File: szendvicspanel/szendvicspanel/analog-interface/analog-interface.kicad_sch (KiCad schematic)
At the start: 12 parts, among them J1 AudioJack3, J4 Conn_01x04_Pin, J5 Conn_01x04_Pin, U3 TL072

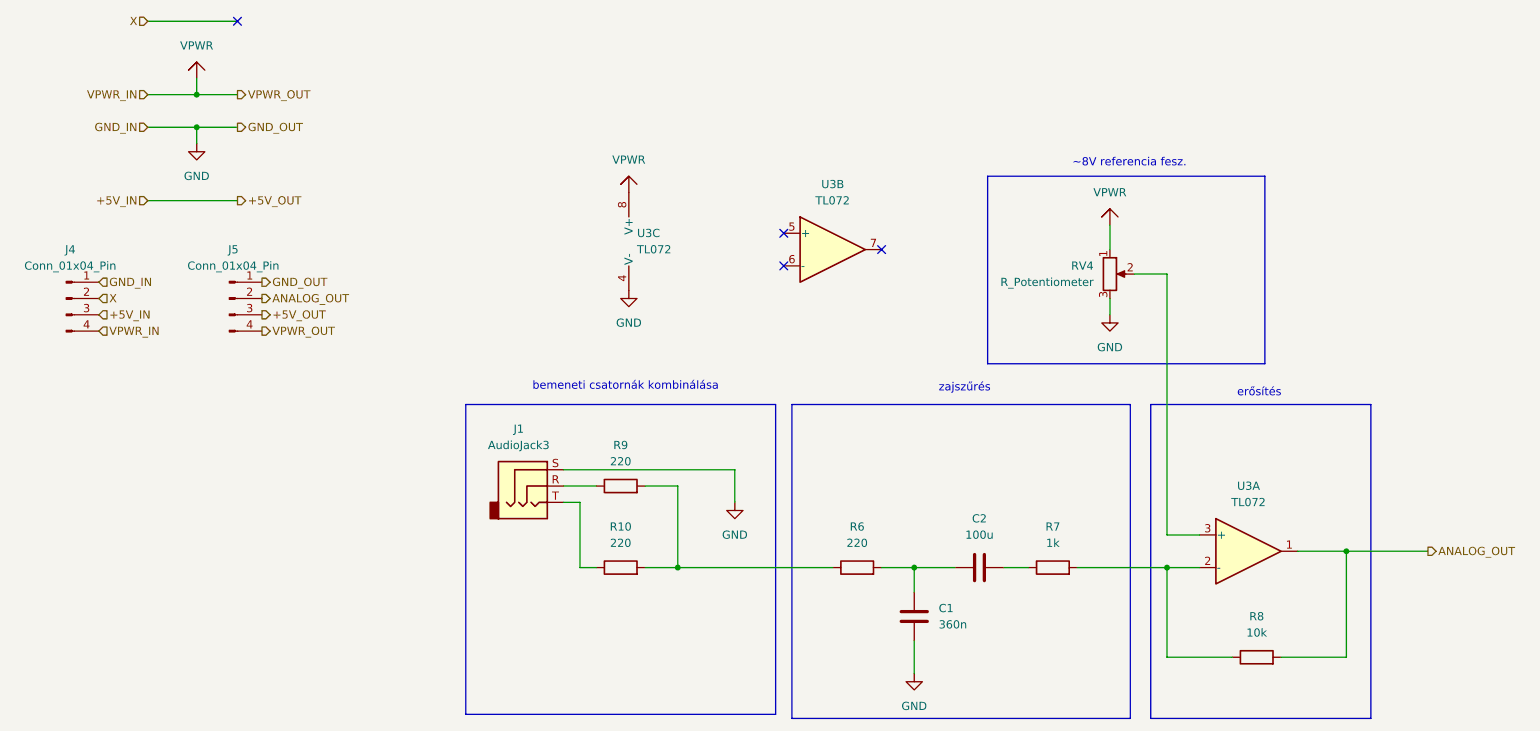
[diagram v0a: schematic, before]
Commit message: Átstrukturálás hierarchikus PCB-hez
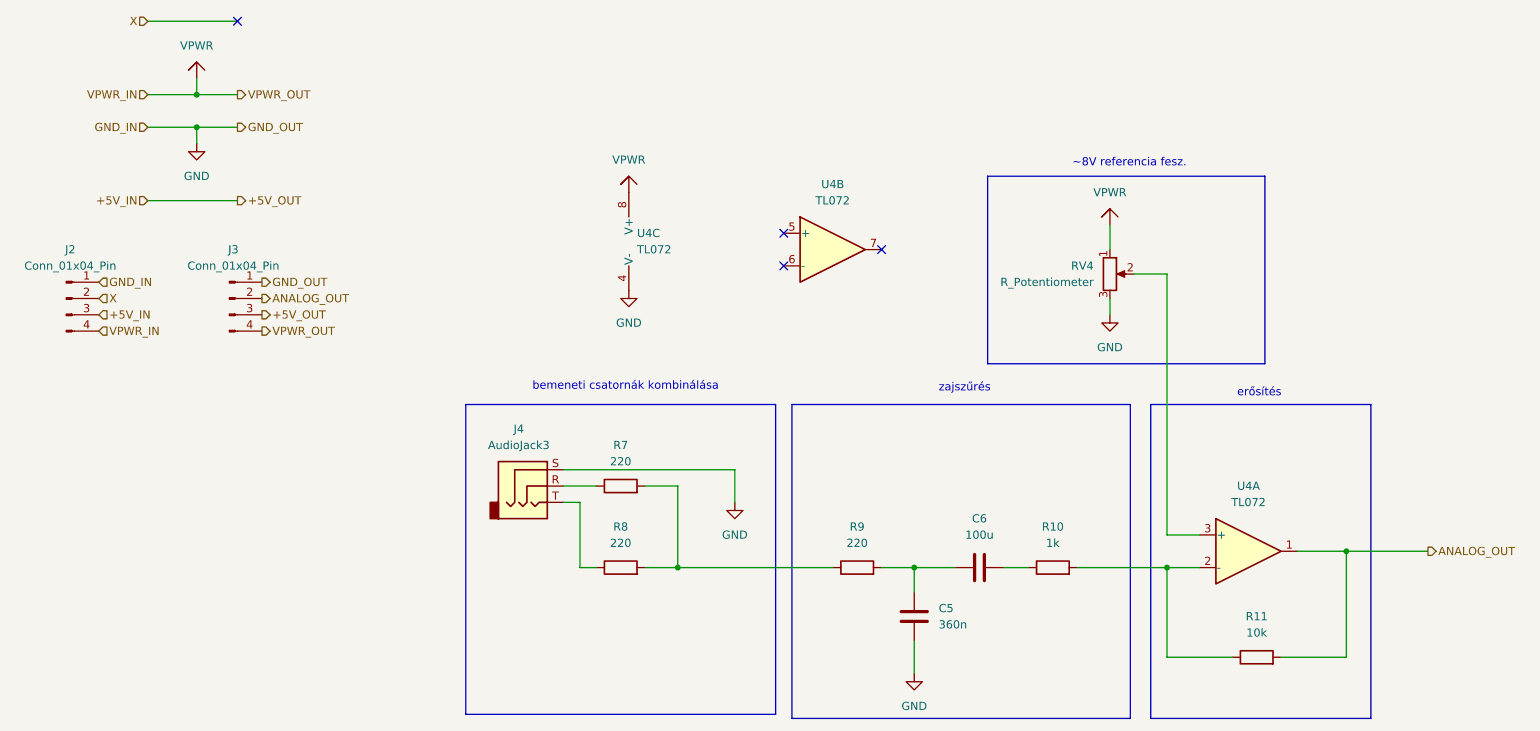
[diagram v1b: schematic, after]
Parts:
- renumbered C1 to C5, C2 to C6, J4 to J2, J5 to J3, J1 to J4, R7 to R10, R8 to R11, R9 to R7, R10 to R8, R6 to R9, U3 to U4
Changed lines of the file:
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@@
 		(dnp no)
 		(fields_autoplaced yes)
-		(property "Reference" "#PWR012"
+		(property "Reference" "#PWR022"
 			(at 186.69 77.47 0)
 			(effects
@@
 			(project "szendvicspanel"
 				(path "/2e536be4-7a69-4064-ab31-c73232c2dcfe/956847b2-170c-4df3-ad01-276d0d878286"
-					(reference "#PWR012")
+					(reference "#PWR022")
 					(unit 1)
 				)
@@
 		(dnp no)
 		(fields_autoplaced yes)
-		(property "Reference" "R9"
+		(property "Reference" "R7"
 			(at 110.49 91.44 90)
 			(effects
@@
 			(project ""
 				(path "/2e536be4-7a69-4064-ab31-c73232c2dcfe/956847b2-170c-4df3-ad01-276d0d878286"
-					(reference "R9")
+					(reference "R7")
 					(unit 1)
 				)
@@
 		(dnp no)
 		(fields_autoplaced yes)
-		(property "Reference" "R6"
+		(property "Reference" "R9"
 			(at 147.32 104.14 90)
 			(effects
@@
 			(project ""
 				(path "/2e536be4-7a69-4064-ab31-c73232c2dcfe/956847b2-170c-4df3-ad01-276d0d878286"
-					(reference "R6")
+					(reference "R9")
 					(unit 1)
 				)
@@
 		(dnp no)
 		(fields_autoplaced yes)
-		(property "Reference" "J5"
+		(property "Reference" "J3"
 			(at 50.165 60.96 0)
 			(effects
@@
 			(project "szendvicspanel"
 				(path "/2e536be4-7a69-4064-ab31-c73232c2dcfe/956847b2-170c-4df3-ad01-276d0d878286"
-					(reference "J5")
+					(reference "J3")
 					(unit 1)
 				)
@@
 		(dnp no)
 		(fields_autoplaced yes)
-		(property "Reference" "R10"
+		(property "Reference" "R8"
 			(at 110.49 104.14 90)
 			(effects
@@
 			(project "szendvicspanel"
 				(path "/2e536be4-7a69-4064-ab31-c73232c2dcfe/956847b2-170c-4df3-ad01-276d0d878286"
-					(reference "R10")
+					(reference "R8")
 					(unit 1)
 				)
@@
 		(on_board yes)
 		(dnp no)
-		(property "Reference" "#PWR020"
+		(property "Reference" "#PWR019"
 			(at 111.76 73.66 0)
 			(effects
@@
 			(project "szendvicspanel"
 				(path "/2e536be4-7a69-4064-ab31-c73232c2dcfe/956847b2-170c-4df3-ad01-276d0d878286"
-					(reference "#PWR020")
+					(reference "#PWR019")
 					(unit 1)
 				)
@@
 		(dnp no)
 		(fields_autoplaced yes)
-		(property "Reference" "C2"
+		(property "Reference" "C6"
 			(at 166.37 102.87 90)
 			(effects
@@
 			(project ""
 				(path "/2e536be4-7a69-4064-ab31-c73232c2dcfe/956847b2-170c-4df3-ad01-276d0d878286"
-					(reference "C2")
+					(reference "C6")
 					(unit 1)
 				)
@@
 		(dnp no)
 		(fields_autoplaced yes)
-		(property "Reference" "U3"
+		(property "Reference" "U4"
 			(at 113.03 58.4199 0)
 			(effects
@@
 			(project ""
 				(path "/2e536be4-7a69-4064-ab31-c73232c2dcfe/956847b2-170c-4df3-ad01-276d0d878286"
-					(reference "U3")
+					(reference "U4")
 					(unit 3)
 				)
@@
 		(dnp no)
 		(fields_autoplaced yes)
-		(property "Reference" "R7"
+		(property "Reference" "R10"
 			(at 177.8 104.14 90)
 			(effects
@@
 			(project ""
 				(path "/2e536be4-7a69-4064-ab31-c73232c2dcfe/956847b2-170c-4df3-ad01-276d0d878286"
-					(reference "R7")
+					(reference "R10")
 					(unit 1)
 				)
@@
 		(dnp no)
 		(fields_autoplaced yes)
-		(property "Reference" "#VPWR09"
+		(property "Reference" "#VPWR07"
 			(at 111.76 52.07 0)
 			(effects
@@
 			(project "szendvicspanel"
 				(path "/2e536be4-7a69-4064-ab31-c73232c2dcfe/956847b2-170c-4df3-ad01-276d0d878286"
-					(reference "#VPWR09")
+					(reference "#VPWR07")
 					(unit 1)
 				)
@@
 		(dnp no)
 		(fields_autoplaced yes)
-		(property "Reference" "#PWR08"
+		(property "Reference" "#PWR021"
 			(at 156.21 133.35 0)
 			(effects
@@
 			(project ""
 				(path "/2e536be4-7a69-4064-ab31-c73232c2dcfe/956847b2-170c-4df3-ad01-276d0d878286"
-					(reference "#PWR08")
+					(reference "#PWR021")
 					(unit 1)
 				)
@@
 		(dnp no)
 		(fields_autoplaced yes)
-		(property "Reference" "J1"
+		(property "Reference" "J4"
 			(at 94.615 88.9 0)
 			(effects
@@
 			(project ""
 				(path "/2e536be4-7a69-4064-ab31-c73232c2dcfe/956847b2-170c-4df3-ad01-276d0d878286"
-					(reference "J1")
+					(reference "J4")
 					(unit 1)
 				)
@@
 		(dnp no)
 		(fields_autoplaced yes)
-		(property "Reference" "#VPWR07"
+		(property "Reference" "#VPWR06"
 			(at 44.45 34.29 0)
 			(effects
@@
 			(project "szendvicspanel"
 				(path "/2e536be4-7a69-4064-ab31-c73232c2dcfe/956847b2-170c-4df3-ad01-276d0d878286"
-					(reference "#VPWR07")
+					(reference "#VPWR06")
 					(unit 1)
 				)
@@
 		(dnp no)
 		(fields_autoplaced yes)
-		(property "Reference" "#PWR011"
+		(property "Reference" "#PWR018"
 			(at 44.45 50.8 0)
 			(effects
@@
 			(project "szendvicspanel"
 				(path "/2e536be4-7a69-4064-ab31-c73232c2dcfe/956847b2-170c-4df3-ad01-276d0d878286"
-					(reference "#PWR011")
+					(reference "#PWR018")
 					(unit 1)
 				)
@@
 		(dnp no)
 		(fields_autoplaced yes)
-		(property "Reference" "U3"
+		(property "Reference" "U4"
 			(at 143.51 50.8 0)
 			(effects
@@
 			(project ""
 				(path "/2e536be4-7a69-4064-ab31-c73232c2dcfe/956847b2-170c-4df3-ad01-276d0d878286"
-					(reference "U3")
+					(reference "U4")
 					(unit 2)
 				)
@@
 		(dnp no)
 		(fields_autoplaced yes)
-		(property "Reference" "U3"
+		(property "Reference" "U4"
 			(at 208.28 97.79 0)
 			(effects
@@
 			(project ""
 				(path "/2e536be4-7a69-4064-ab31-c73232c2dcfe/956847b2-170c-4df3-ad01-276d0d878286"
-					(reference "U3")
+					(reference "U4")
 					(unit 1)
 				)
@@
 		(on_board yes)
 		(dnp no)
-		(property "Reference" "#PWR019"
+		(property "Reference" "#PWR020"
 			(at 128.27 106.68 0)
 			(effects
@@
 			(project "szendvicspanel"
 				(path "/2e536be4-7a69-4064-ab31-c73232c2dcfe/956847b2-170c-4df3-ad01-276d0d878286"
-					(reference "#PWR019")
+					(reference "#PWR020")
 					(unit 1)
 				)
@@
 		(dnp no)
 		(fields_autoplaced yes)
-		(property "Reference" "J4"
+		(property "Reference" "J2"
 			(at 24.765 60.96 0)
 			(effects
@@
 			(project "szendvicspanel"
 				(path "/2e536be4-7a69-4064-ab31-c73232c2dcfe/956847b2-170c-4df3-ad01-276d0d878286"
-					(reference "J4")
+					(reference "J2")
 					(unit 1)
 				)
@@
 		(dnp no)
 		(fields_autoplaced yes)
-		(property "Reference" "C1"
+		(property "Reference" "C5"
 			(at 160.02 116.8399 0)
 			(effects
@@
 			(project ""
 				(path "/2e536be4-7a69-4064-ab31-c73232c2dcfe/956847b2-170c-4df3-ad01-276d0d878286"
-					(reference "C1")
+					(reference "C5")
 					(unit 1)
 				)
@@
 		(dnp no)
 		(fields_autoplaced yes)
-		(property "Reference" "R8"
+		(property "Reference" "R11"
 			(at 209.55 118.11 90)
 			(effects
@@
 			(project ""
 				(path "/2e536be4-7a69-4064-ab31-c73232c2dcfe/956847b2-170c-4df3-ad01-276d0d878286"
-					(reference "R8")
-					(unit 1)
-				)
+					(reference "R11")
+					(unit 1)
+				)
